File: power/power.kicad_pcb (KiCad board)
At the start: 4 copper layers, 75 x 56 mm, 66 parts, among them J1 GPIO, J10 SCL1, J11 SDA1, J12 SCL2, J13 SDA2, J14 VCC1, J15 GND1, J16 VCC2, J17 GND2, J18 JP_VCC_PWM, J19 Conn_01x01, J2 PWM_OUT, J3 PWM_IN, J4 JP_EXT, J5 JP_VOLTS, J6 I2C_EXT1, J7 I2C_EXT2, J8 PWM_OUT, J9 JP_VCC_PWM, Q1 D15P05, Q2 BC847C, U2 REF5050IDGK, U3 L78L06_SOT89, U5 TPS56A37RPAR

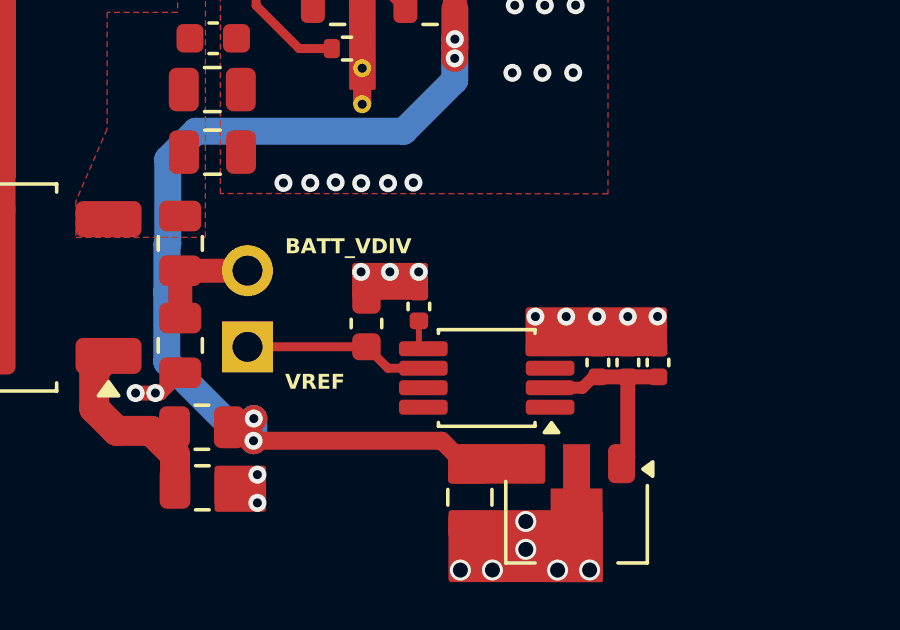
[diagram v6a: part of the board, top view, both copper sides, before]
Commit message: use 0603 for 1uF; correct dates
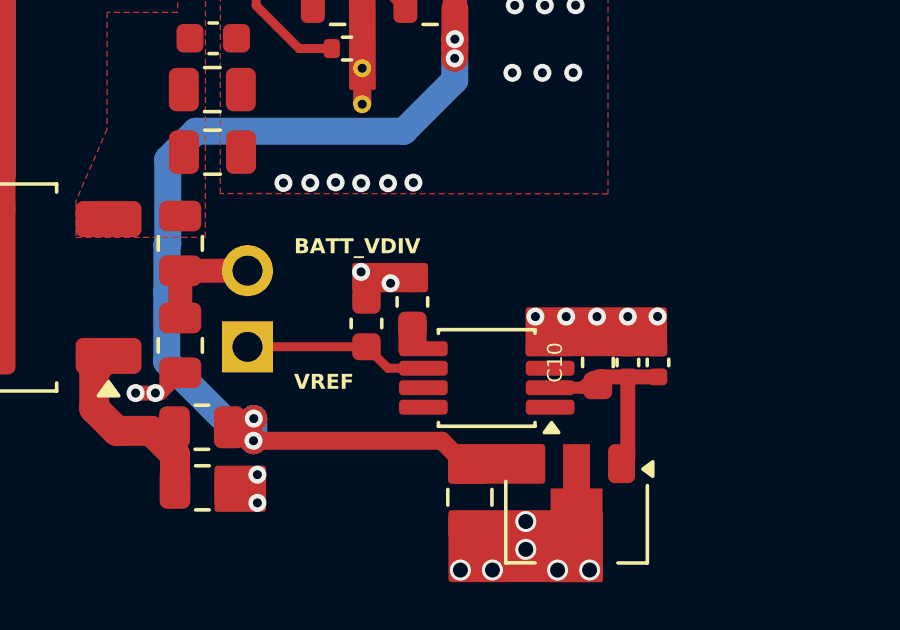
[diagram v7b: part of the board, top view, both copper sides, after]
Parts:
- C10, C7: value 1uF (105) 10% 25V -> 1uF (105) 10% 50V; footprint Capacitor_SMD:C_0402_1005Metric -> Capacitor_SMD:C_0603_1608Metric
- moved C7 0.26 mm to (120.1, 88.5)
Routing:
- net Net-(U2-Trim/NR): track 1.04 -> 0.00 mm
- net GND: vias 79 -> 78

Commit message: texts
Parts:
- moved C7 0.45 mm to (120.1, 88.1)
- moved C9 0.40 mm to (127.7, 90.5)
- moved C12 0.35 mm to (128.6, 90.5)
- moved C10 0.20 mm to (126.5, 90.5)
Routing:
- net +3V3: track 56.4 -> 61.4 mm
- net +6V: track 6.94 -> 7.85 mm
- net /VIN: track 33.9 -> 34.8 mm, vias 4 -> 6
- net GND: track 4.85 -> 5.61 mm
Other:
- board text added: "closed = Buzzer open = PWM"
- board text removed: "closed = Buzzer open = PWM0"
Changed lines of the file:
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@@
 		)
 		(fp_text user "3"
-			(at 2.6 0 0)
+			(at 2.6 1.119693 0)
 			(layer "F.SilkS")
 			(effects
@@
 		)
 		(fp_text user "1"
-			(at -2.6 0 0)
+			(at -2.6 1.119693 0)
 			(layer "F.SilkS")
 			(effects
@@
 	(footprint "Capacitor_SMD:C_0603_1608Metric"
 		(layer "F.Cu")
-		(at 120.096867 88.50112 90)
+		(at 120.096867 88.05112 90)
 		(descr "Capacitor SMD 0603 (1608 Metric), square (rectangular) end terminal, IPC-7351 nominal, (Body size source: IPC-SM-782 page 76, https://www.pcb-3d.com/wordpress/wp-content/uploads/ipc-sm-782a_amendment_1_and_2.pdf)")
 		(tags "capacitor")
@@
 	(footprint "Capacitor_SMD:C_0402_1005Metric"
 		(layer "F.Cu")
-		(at 127.279764 90.520617 90)
+		(at 127.679764 90.520617 90)
 		(descr "Capacitor SMD 0402 (1005 Metric), square (rectangular) end terminal, IPC-7351 nominal, (Body size source: IPC-SM-782 page 76, https://www.pcb-3d.com/wordpress/wp-content/uploads/ipc-sm-782a_amendment_1_and_2.pdf)")
 		(tags "capacitor")
@@
 	(footprint "Capacitor_SMD:C_0402_1005Metric"
 		(layer "F.Cu")
-		(at 128.283153 90.520089 90)
+		(at 128.633153 90.520089 90)
 		(descr "Capacitor SMD 0402 (1005 Metric), square (rectangular) end terminal, IPC-7351 nominal, (Body size source: IPC-SM-782 page 76, https://www.pcb-3d.com/wordpress/wp-content/uploads/ipc-sm-782a_amendment_1_and_2.pdf)")
 		(tags "capacitor")
@@
 	(footprint "Capacitor_SMD:C_0603_1608Metric"
 		(layer "F.Cu")
-		(at 126.279764 90.520617 90)
+		(at 126.479764 90.520617 90)
 		(descr "Capacitor SMD 0603 (1608 Metric), square (rectangular) end terminal, IPC-7351 nominal, (Body size source: IPC-SM-782 page 76, https://www.pcb-3d.com/wordpress/wp-content/uploads/ipc-sm-782a_amendment_1_and_2.pdf)")
 		(tags "capacitor")
@@
 			(at 0 -1.43 90)
 			(layer "F.SilkS")
+			(hide yes)
 			(effects
 				(font
@@
 	)
 	(gr_rect
-		(start 118.186406 87.30086)
-		(end 120.516406 88.08)
+		(start 118.186406 86.95)
+		(end 120.516406 87.7)
 		(stroke
 			(width 0.2)
@@
 	(gr_rect
 		(start 123.966406 88.78086)
-		(end 128.486406 90.21086)
+		(end 128.85 90.21086)
 		(stroke
 			(width 0.2)
@@
 	)
 	(gr_text "BATT_VDIV"
-		(at 116.15 86.94 0)
+		(at 116.15 86.39 0)
 		(layer "F.SilkS")
 		(effects
@@
 		)
 	)
-	(gr_text "closed = Buzzer\nopen = PWM0"
+	(gr_text "closed = Buzzer\nopen = PWM"
 		(at 149.005 60.03 0)
 		(layer "F.SilkS")
@@
 	)
 	(segment
-		(start 125.767376 91.361598)
-		(end 124.686318 91.361598)
-		(width 0.4)
+		(start 126.279764 91.000617)
+		(end 126.401813 91.000617)
+		(width 0.5)
 		(layer "F.Cu")
 		(net "+6V")
 	)
 	(segment
-		(start 126.279764 91.000617)
-		(end 126.401813 91.000617)
+		(start 128.632625 91.000617)
+		(end 128.633153 91.000089)
 		(width 0.5)
 		(layer "F.Cu")
@@
 	)
 	(segment
-		(start 127.276406 91.00086)
-		(end 127.276406 93.685086)
+		(start 128.633153 91.000089)
+		(end 128.283153 91.000089)
 		(width 0.5)
 		(layer "F.Cu")
@@
 	)
 	(segment
-		(start 127.220881 93.740611)
-		(end 127.068469 93.893023)
+		(start 127.026406 91.00086)
+		(end 127.026406 93.685086)
 		(width 0.5)
 		(layer "F.Cu")
@@
 	)
 	(segment
-		(start 128.282625 91.000617)
-		(end 128.283153 91.000089)
+		(start 127.220881 93.740611)
+		(end 127.068469 93.893023)
 		(width 0.5)
 		(layer "F.Cu")
@@
 	)
 	(segment
-		(start 127.279764 91.000617)
-		(end 128.282625 91.000617)
-		(width 0.5)
+		(start 126.279764 91.000617)
+		(end 126.279764 91.361598)
+		(width 0.4)
 		(layer "F.Cu")
 		(net "+6V")
 	)
 	(segment
-		(start 126.128357 91.000617)
-		(end 125.767376 91.361598)
+		(start 126.279764 91.361598)
+		(end 124.686318 91.361598)
 		(width 0.4)
 		(layer "F.Cu")
@@
 	)
 	(segment
-		(start 126.279764 91.000617)
-		(end 126.128357 91.000617)
-		(width 0.4)
+		(start 127.276406 93.685086)
+		(end 127.068469 93.893023)
+		(width 0.5)
 		(layer "F.Cu")
 		(net "+6V")
 	)
 	(segment
-		(start 127.276406 93.685086)
-		(end 127.068469 93.893023)
+		(start 127.279764 91.000617)
+		(end 128.632625 91.000617)
 		(width 0.5)
 		(layer "F.Cu")
@@
 	)
 	(segment
+		(start 118.564664 88.44586)
+		(end 118.564664 87.679118)
+		(width 1)
+		(layer "F.Cu")
+		(net "GND")
+	)
+	(segment
 		(start 111.683711 91.54)
 		(end 112.36 90.863711)
@@
 	)
 	(via
-		(at 119.37 87.88)
+		(at 119.22 87.48)
 		(size 0.6)
 		(drill 0.3)
@@
 	)
 	(via
+		(at 111.942983 84.65)
+		(size 0.6)
+		(drill 0.3)
+		(layers "F.Cu" "B.Cu")
+		(net "/VIN")
+	)
+	(via
 		(at 121.507178 80.383847)
 		(size 0.6)
@@
 	)
 	(via
+		(at 111.1 84.65)
+		(size 0.6)
+		(drill 0.3)
+		(layers "F.Cu" "B.Cu")
+		(free yes)
+		(net "/VIN")
+	)
+	(via
 		(at 114.81 92.39)
 		(size 0.6)
@@
 	(segment
 		(start 111.942983 86.568918)
-		(end 111.942983 83.74763)
+		(end 111.942983 84.65)
 		(width 0.9)
 		(layer "B.Cu")
@@
 	)
 	(segment
+		(start 111.942983 84.65)
+		(end 111.942983 83.74763)
+		(width 0.9)
+		(layer "B.Cu")
+		(net "/VIN")
+	)
+	(segment
+		(start 111.942983 84.65)
+		(end 111.1 84.65)
+		(width 0.9)
+		(layer "B.Cu")
+		(net "/VIN")
+	)
+	(segment
 		(start 114.81 93.12)
 		(end 114.8 93.13)
@@
 		(layer "B.Cu")
 		(net "+3V3")
+	)
+	(segment
+		(start 104.959832 52.890168)
+		(end 106.87 50.98)
+		(width 0.5)
+		(layer "B.Cu")
+		(net "+3V3")
+	)
+	(segment
+		(start 106.87 50.98)
+		(end 107.855 50.98)
+		(width 0.5)
+		(layer "B.Cu")
+		(net "+3V3")
+	)
+	(segment
+		(start 103.604915 52.890168)
+		(end 104.959832 52.890168)
+		(width 0.5)
+		(layer "B.Cu")
+		(net "+3V3")
